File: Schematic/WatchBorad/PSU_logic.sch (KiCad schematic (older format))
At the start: 37 parts, among them J3 TYPE-C-31-M-17, SW1 SW_Push, SW2 SW_Push, U10 M41T62Q6F, U5 BQ21040DBVT, U6 MAX17048G+T10, U7 max16054azt+t, U8 TPS2113APWR, Y1 Crystal_Small

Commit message: Added missed resistors to the lcsc [SCHEMATIC][BOM]
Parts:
- R1, R15, R16, R17, R18, R2, R20, R21, R23, R24: lcsc (none) -> https://www.lcsc.com/product-detail/Chip-Resistor-Surface-M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
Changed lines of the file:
@@
 F 2 "Resistor_SMD:R_0603_1608Metric" V 4430 1350 50  0001 C CNN
 F 3 "~" H 4500 1350 50  0001 C CNN
+F 4 "https://www.lcsc.com/product-detail/Chip-Resistor-Surface-Mount_YAGEO-RC0603FR-0710KL_C98220.html" H 4500 1350 50  0001 C CNN "lcsc"
 	1    4500 1350
 	0    1    1    0
@@
 F 2 "Resistor_SMD:R_0603_1608Metric" V 2380 2650 50  0001 C CNN
 F 3 "~" H 2450 2650 50  0001 C CNN
+F 4 "https://www.lcsc.com/product-detail/Chip-Resistor-Surface-Mount_YAGEO-RC0603FR-0710KL_C98220.html" H 2450 2650 50  0001 C CNN "lcsc"
 	1    2450 2650
 	-1   0    0    1
@@
 F 2 "Resistor_SMD:R_0603_1608Metric" V 2555 1975 50  0001 C CNN
 F 3 "~" H 2625 1975 50  0001 C CNN
+F 4 "https://www.lcsc.com/product-detail/Chip-Resistor-Surface-Mount_YAGEO-RC0603FR-0710KL_C98220.html" H 2625 1975 50  0001 C CNN "lcsc"
 	1    2625 1975
 	-1   0    0    1
@@
 F 2 "Resistor_SMD:R_0603_1608Metric" V 7955 6075 50  0001 C CNN
 F 3 "https://lcsc.com/product-detail/Others_Viking-Tech-ARG03FTC3300_C217969.html" H 8025 6075 50  0001 C CNN
+F 4 "https://www.lcsc.com/product-detail/Chip-Resistor-Surface-Mount_Walsin-Tech-Corp-WR06X331JTL_C384242.html" H 8025 6075 50  0001 C CNN "lcsc"
 	1    8025 6075
 	0    1    1    0
@@
 F 2 "Resistor_SMD:R_0603_1608Metric" V 2680 4850 50  0001 C CNN
 F 3 "~" H 2750 4850 50  0001 C CNN
+F 4 "https://www.lcsc.com/product-detail/Chip-Resistor-Surface-Mount_YAGEO-RC0603FR-0710KL_C98220.html" H 2750 4850 50  0001 C CNN "lcsc"
 	1    2750 4850
 	0    1    -1   0
@@
 F 2 "Resistor_SMD:R_0603_1608Metric" V 4955 4800 50  0001 C CNN
 F 3 "~" H 5025 4800 50  0001 C CNN
+F 4 "https://www.lcsc.com/product-detail/Chip-Resistor-Surface-Mount_YAGEO-RC0603FR-0710KL_C98220.html" H 5025 4800 50  0001 C CNN "lcsc"
 	1    5025 4800
 	1    0    0    1
@@
 F 2 "Resistor_SMD:R_0603_1608Metric" V 1405 1725 50  0001 C CNN
 F 3 "https://lcsc.com/product-detail/Others_Viking-Tech-ARG03FTC3300_C217969.html" H 1475 1725 50  0001 C CNN
+F 4 "https://www.lcsc.com/product-detail/Chip-Resistor-Surface-Mount_Walsin-Tech-Corp-WR06X331JTL_C384242.html" H 1475 1725 50  0001 C CNN "lcsc"
 	1    1475 1725
 	0    1    1    0
@@
 F 2 "Resistor_SMD:R_0603_1608Metric" V 1405 2350 50  0001 C CNN
 F 3 "https://lcsc.com/product-detail/Others_Viking-Tech-ARG03FTC3300_C217969.html" H 1475 2350 50  0001 C CNN
+F 4 "https://www.lcsc.com/product-detail/Chip-Resistor-Surface-Mount_Walsin-Tech-Corp-WR06X331JTL_C384242.html" H 1475 2350 50  0001 C CNN "lcsc"
 	1    1475 2350
 	0    1    1    0
@@
 F 2 "Resistor_SMD:R_0603_1608Metric" V 10305 2400 50  0001 C CNN
 F 3 "~" H 10375 2400 50  0001 C CNN
+F 4 "https://www.lcsc.com/product-detail/Chip-Resistor-Surface-Mount_YAGEO-RC0603FR-0710KL_C98220.html" H 10375 2400 50  0001 C CNN "lcsc"
 	1    10375 2400
 	1    0    0    -1
@@
 F 2 "Resistor_SMD:R_0603_1608Metric" V 8255 2300 50  0001 C CNN
 F 3 "~" H 8325 2300 50  0001 C CNN
+F 4 "https://www.lcsc.com/product-detail/Chip-Resistor-Surface-Mount_YAGEO-RC0603FR-0710KL_C98220.html" H 8325 2300 50  0001 C CNN "lcsc"
 	1    8325 2300
 	1    0    0    -1

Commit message: Added D-trigger instead of the MAX switching chip
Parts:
- removed U7: max16054azt+t, TO_SOT_Packages_SMD:SOT-23-6_Handsoldering, symbol OnOffControllers:max16054azt+t
- added C8: 100 nF, Capacitor_SMD:C_0603_1608Metric, symbol Device:C
- added U7: SN74LVC2G74-EP_DCU_8, SN74LVC2G74:SN74LVC2G74, symbol SN74LVC2G74:SN74LVC2G74-EP_DCU_8
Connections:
- wire segments 147 -> 158
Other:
- note removed: "Int 63KOhm PU\n"
- moved on the sheet: C29, R21, TP11, TP20

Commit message: Removed redundant symbols descriptions from schematic [SCHEMATIC]
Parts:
- U10: MPN M41T62Q6F -> (none); OC_FARNELL 1224441 -> (none); OC_NEWARK 56P9316 -> (none); PACKAGE QFN-16 -> (none); SUPPLIER STMICROELECTRONICS -> (none)
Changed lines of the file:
@@
 F 2 "QFN50P300X300X100-17N" H 9475 3050 50  0001 L BNN
 F 3 "https://datasheet.lcsc.com/lcsc/1806121917_STMicroelectronics-M41T62Q6F_C113207.pdf" H 9475 3050 50  0001 L BNN
-F 4 "M41T62Q6F" H 9475 3050 50  0001 L BNN "MPN"
-F 5 "1224441" H 9475 3050 50  0001 L BNN "OC_FARNELL"
-F 6 "56P9316" H 9475 3050 50  0001 L BNN "OC_NEWARK"
-F 7 "QFN-16" H 9475 3050 50  0001 L BNN "PACKAGE"
-F 8 "STMICROELECTRONICS" H 9475 3050 50  0001 L BNN "SUPPLIER"
-F 9 "https://lcsc.com/product-detail/Real-time-Clocks-span-style-background-color-ff0-RTC-span_STMicroelectronics-M41T62Q6F_C113207.html" H 9475 3050 50  0001 C CNN "lcsc"
+F 4 "https://lcsc.com/product-detail/Real-time-Clocks-span-style-background-color-ff0-RTC-span_STMicroelectronics-M41T62Q6F_C113207.html" H 9475 3050 50  0001 C CNN "lcsc"
 	1    9475 3050
 	1    0    0    -1

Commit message: Fixed D-trigger routing around the switching circuit [PCB]
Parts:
- added R22, R25: 10k, Resistor_SMD:R_0603_1608Metric, symbol Device:R
- C8: value 100 nF -> 10 uF
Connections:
- wire segments 158 -> 164
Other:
- moved on the sheet: C29, C8, R21
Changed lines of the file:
@@
 L Device:C C?
 U 1 1 5F943E27
-P 7110 1300
+P 7630 1300
 AR Path="/5EA4867C/5F943E27" Ref="C?"  Part="1"
 AR Path="/5E9C1C3A/5F943E27" Ref="C?"  Part="1"
 AR Path="/5ED3F98E/5F943E27" Ref="C?"  Part="1"
 AR Path="/5F913559/5F943E27" Ref="C29"  Part="1"
-F 0 "C29" H 7135 1375 50  0000 L CNN
-F 1 "100 nF" V 6960 1175 50  0000 L CNN
-F 2 "Capacitor_SMD:C_0603_1608Metric" H 7148 1150 50  0001 C CNN
-F 3 "~" H 7110 1300 50  0001 C CNN
-F 4 "https://lcsc.com/product-detail/Multilayer-Ceramic-Capacitors-MLCC-SMD-SMT_YAGEO-CC0603KRX7R9BB104_C14663.html" H 7110 1300 50  0001 C CNN "lcsc"
-	1    7110 1300
+F 0 "C29" H 7655 1375 50  0000 L CNN
+F 1 "100 nF" V 7480 1175 50  0000 L CNN
+F 2 "Capacitor_SMD:C_0603_1608Metric" H 7668 1150 50  0001 C CNN
+F 3 "~" H 7630 1300 50  0001 C CNN
+F 4 "https://lcsc.com/product-detail/Multilayer-Ceramic-Capacitors-MLCC-SMD-SMT_YAGEO-CC0603KRX7R9BB104_C14663.html" H 7630 1300 50  0001 C CNN "lcsc"
+	1    7630 1300
 	0    -1   -1   0
 $EndComp
-Text Label 6420 1300 0    50   ~ 0
+Text Label 6940 1300 0    50   ~ 0
 V_Battery_P
 Wire Notes Line
@@
 L power:GND #PWR?
 U 1 1 5F943EB2
-P 7000 2600
+P 6800 2740
 AR Path="/5F943EB2" Ref="#PWR?"  Part="1"
 AR Path="/5E9B1DCE/5F943EB2" Ref="#PWR?"  Part="1"
 AR Path="/5ED3F98E/5F943EB2" Ref="#PWR?"  Part="1"
 AR Path="/5F913559/5F943EB2" Ref="#PWR035"  Part="1"
-F 0 "#PWR035" H 7000 2350 50  0001 C CNN
-F 1 "GND" H 7000 2450 50  0000 C CNN
-F 2 "" H 7000 2600 50  0001 C CNN
-F 3 "" H 7000 2600 50  0001 C CNN
-	1    7000 2600
+F 0 "#PWR035" H 6800 2490 50  0001 C CNN
+F 1 "GND" H 6800 2590 50  0000 C CNN
+F 2 "" H 6800 2740 50  0001 C CNN
+F 3 "" H 6800 2740 50  0001 C CNN
+	1    6800 2740
 	1    0    0    -1
 $EndComp
@@
 L power:+BATT #PWR?
 U 1 1 5F9B18FF
-P 6900 1140
+P 7420 1140
 AR Path="/5E9C1C3A/5F9B18FF" Ref="#PWR?"  Part="1"
 AR Path="/5F7F86D0/5F9B18FF" Ref="#PWR?"  Part="1"
 AR Path="/5ED3F98E/5F9B18FF" Ref="#PWR?"  Part="1"
 AR Path="/5F913559/5F9B18FF" Ref="#PWR036"  Part="1"
-F 0 "#PWR036" H 6900 990 50  0001 C CNN
-F 1 "+BATT" H 6915 1313 50  0000 C CNN
-F 2 "" H 6900 1140 50  0001 C CNN
-F 3 "" H 6900 1140 50  0001 C CNN
-	1    6900 1140
+F 0 "#PWR036" H 7420 990 50  0001 C CNN
+F 1 "+BATT" H 7435 1313 50  0000 C CNN
+F 2 "" H 7420 1140 50  0001 C CNN
+F 3 "" H 7420 1140 50  0001 C CNN
+	1    7420 1140
 	-1   0    0    -1
 $EndComp
@@
 	6840 3340 6840 3520
 Wire Wire Line
-	3150 1300 4170 1300
-Wire Wire Line
 	3150 1300 3150 1525
 $Comp
 L power:GND #PWR0102
 U 1 1 6187DAB4
-P 7360 1300
-F 0 "#PWR0102" H 7360 1050 50  0001 C CNN
-F 1 "GND" H 7365 1127 50  0000 C CNN
-F 2 "" H 7360 1300 50  0001 C CNN
-F 3 "" H 7360 1300 50  0001 C CNN
-	1    7360 1300
+P 7880 1300
+F 0 "#PWR0102" H 7880 1050 50  0001 C CNN
+F 1 "GND" H 7885 1127 50  0000 C CNN
+F 2 "" H 7880 1300 50  0001 C CNN
+F 3 "" H 7880 1300 50  0001 C CNN
+	1    7880 1300
 	0    -1   -1   0
 $EndComp
@@
 	4100 1400 4170 1400
 Wire Wire Line
-	6370 1300 6900 1300
-Wire Wire Line
-	6900 1140 6900 1300
-Connection ~ 6900 1300
-Wire Wire Line
-	6900 1300 6960 1300
-Wire Wire Line
-	7260 1300 7360 1300
+	7420 1140 7420 1300
+Connection ~ 7420 1300
+Wire Wire Line
+	7420 1300 7480 1300
+Wire Wire Line
+	7780 1300 7880 1300
 $Comp
 L Connector:TestPoint TP?
@@
 L Device:C C8
 U 1 1 6189A4CE
-P 7000 2350
-F 0 "C8" H 7115 2396 50  0000 L CNN
-F 1 "100 nF" H 7115 2305 50  0000 L CNN
-F 2 "Capacitor_SMD:C_0603_1608Metric" H 7038 2200 50  0001 C CNN
-F 3 "~" H 7000 2350 50  0001 C CNN
-F 4 "https://lcsc.com/product-detail/Multilayer-Ceramic-Capacitors-MLCC-SMD-SMT_YAGEO-CC0603KRX7R9BB104_C14663.html" H 7000 2350 50  0001 C CNN "lcsc"
-	1    7000 2350
+P 6800 2490
+F 0 "C8" H 6915 2536 50  0000 L CNN
+F 1 "10 uF" H 6915 2445 50  0000 L CNN
+F 2 "Capacitor_SMD:C_0603_1608Metric" H 6838 2340 50  0001 C CNN
+F 3 "~" H 6800 2490 50  0001 C CNN
+F 4 "https://lcsc.com/product-detail/Multilayer-Ceramic-Capacitors-MLCC-SMD-SMT_YAGEO-CC0603KRX7R9BB104_C14663.html" H 6800 2490 50  0001 C CNN "lcsc"
+	1    6800 2490
 	1    0    0    -1
 $EndComp
@@
 L Device:R R?
 U 1 1 5F943E4B
-P 6660 2110
+P 6800 2100
 AR Path="/5EA4867C/5F943E4B" Ref="R?"  Part="1"
 AR Path="/5ED3F98E/5F943E4B" Ref="R?"  Part="1"
 AR Path="/5F913559/5F943E4B" Ref="R21"  Part="1"
-F 0 "R21" V 6560 1910 50  0000 L CNN
-F 1 "10k" V 6560 2210 50  0000 L CNN
-F 2 "Resistor_SMD:R_0603_1608Metric" V 6590 2110 50  0001 C CNN
-F 3 "~" H 6660 2110 50  0001 C CNN
-F 4 "https://www.lcsc.com/product-detail/Chip-Resistor-Surface-Mount_YAGEO-RC0603FR-0710KL_C98220.html" H 6660 2110 50  0001 C CNN "lcsc"
-	1    6660 2110
-	0    1    1    0
+F 0 "R21" V 6700 1900 50  0000 L CNN
+F 1 "10k" V 6700 2200 50  0000 L CNN
+F 2 "Resistor_SMD:R_0603_1608Metric" V 6730 2100 50  0001 C CNN
+F 3 "~" H 6800 2100 50  0001 C CNN
+F 4 "https://www.lcsc.com/product-detail/Chip-Resistor-Surface-Mount_YAGEO-RC0603FR-0710KL_C98220.html" H 6800 2100 50  0001 C CNN "lcsc"
+	1    6800 2100
+	-1   0    0    1
 $EndComp
 $Comp
 L power:+BATT #PWR0106
 U 1 1 61996A40
-P 7000 2050
-F 0 "#PWR0106" H 7000 1900 50  0001 C CNN
-F 1 "+BATT" H 7015 2223 50  0000 C CNN
-F 2 "" H 7000 2050 50  0001 C CNN
-F 3 "" H 7000 2050 50  0001 C CNN
-	1    7000 2050
-	1    0    0    -1
-$EndComp
-Wire Wire Line
-	6450 1500 6450 2110
-Wire Wire Line
-	6450 2110 6510 2110
+P 6800 1910
+F 0 "#PWR0106" H 6800 1760 50  0001 C CNN
+F 1 "+BATT" H 6815 2083 50  0000 C CNN
+F 2 "" H 6800 1910 50  0001 C CNN
+F 3 "" H 6800 1910 50  0001 C CNN
+	1    6800 1910
+	1    0    0    -1
+$EndComp
 Wire Wire Line
 	6370 1500 6450 1500
 Wire Wire Line
-	7000 2110 7000 2200
-Wire Wire Line
-	6810 2110 7000 2110
-Wire Wire Line
-	7000 2110 7000 2050
-Connection ~ 7000 2110
-Wire Wire Line
-	7000 2500 7000 2600
+	6800 2640 6800 2740
 $Comp
 L SN74LVC2G74:SN74LVC2G74-EP_DCU_8 U7
@@
 	1    0    0    -1
 $EndComp
+$Comp
+L Device:R R22
+U 1 1 617EFB8E
+P 3690 1110
+F 0 "R22" H 3760 1156 50  0000 L CNN
+F 1 "10k" H 3760 1065 50  0000 L CNN
+F 2 "Resistor_SMD:R_0603_1608Metric" V 3620 1110 50  0001 C CNN
+F 3 "~" H 3690 1110 50  0001 C CNN
+F 4 "https://www.lcsc.com/product-detail/Chip-Resistor-Surface-Mount_YAGEO-RC0603FR-0710KL_C98220.html" H 3690 1110 50  0001 C CNN "lcsc"
+	1    3690 1110
+	1    0    0    -1
+$EndComp
+$Comp
+L power:+BATT #PWR043
+U 1 1 617FFD22
+P 3690 910
+F 0 "#PWR043" H 3690 760 50  0001 C CNN
+F 1 "+BATT" H 3705 1083 50  0000 C CNN
+F 2 "" H 3690 910 50  0001 C CNN
+F 3 "" H 3690 910 50  0001 C CNN
+	1    3690 910
+	1    0    0    -1
+$EndComp
+Wire Wire Line
+	3150 1300 3690 1300
+Wire Wire Line
+	3690 1260 3690 1300
+Connection ~ 3690 1300
+Wire Wire Line
+	3690 1300 4170 1300
+Wire Wire Line
+	3690 910  3690 960
+Wire Wire Line
+	6800 1910 6800 1950
+Wire Wire Line
+	6450 2290 6800 2290
+Wire Wire Line
+	6800 2290 6800 2250
+Wire Wire Line
+	6450 1500 6450 2290
+Wire Wire Line
+	6800 2290 6800 2340
+Connection ~ 6800 2290
+$Comp
+L Device:R R25
+U 1 1 61851142
+P 6480 1090
+F 0 "R25" H 6550 1136 50  0000 L CNN
+F 1 "10k" H 6550 1045 50  0000 L CNN
+F 2 "Resistor_SMD:R_0603_1608Metric" V 6410 1090 50  0001 C CNN
+F 3 "~" H 6480 1090 50  0001 C CNN
+F 4 "https://www.lcsc.com/product-detail/Chip-Resistor-Surface-Mount_YAGEO-RC0603FR-0710KL_C98220.html" H 6480 1090 50  0001 C CNN "lcsc"
+	1    6480 1090
+	1    0    0    -1
+$EndComp
+Wire Wire Line
+	6370 1300 7420 1300
+Wire Wire Line
+	6370 1400 6480 1400
+$Comp
+L power:+BATT #PWR059
+U 1 1 61870E94
+P 6480 890
+F 0 "#PWR059" H 6480 740 50  0001 C CNN
+F 1 "+BATT" H 6495 1063 50  0000 C CNN
+F 2 "" H 6480 890 50  0001 C CNN
+F 3 "" H 6480 890 50  0001 C CNN
+	1    6480 890
+	1    0    0    -1
+$EndComp
+Wire Wire Line
+	6480 940  6480 890
+Wire Wire Line
+	6480 1400 6480 1240
 $EndSCHEMATC

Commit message: Changed Power MUX circuit to the transistors
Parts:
- removed C30, C31: 100 nF, Capacitor_SMD:C_0603_1608Metric, symbol Device:C
- removed U8: TPS2113APWR, LocalFootprints:TPS2115APWR, symbol WatchBorad-rescue:TPS2113APWR-PowerMuxes-WatchBorad-rescue-WatchBorad-rescue
- added D3: D, Diode_SMD:D_0603_1608Metric_Pad1.05x0.95mm_HandSolder, symbol Device:D
- added R34: 10K, Resistor_SMD:R_0603_1608Metric, symbol Device:R
- added VT3, VT5: HX2301A, Package_TO_SOT_SMD:SOT-23, symbol MosfetLocal:HX2301A
- R24: value 330 -> 1K; lcsc https://www.lcsc.com/product-detail/Chip-Resistor-Surface-Mount_Walsin-Tech-Corp-WR06X331JTL_C384242.html -> https://www.lcsc.com/product-detail/Chip-Resistor-Surface-Mount_YAGEO-RC0603FR-0710KL_C98220.html
- VT1, VT2: footprint TO_SOT_Packages_SMD:SOT-23 -> Package_TO_SOT_SMD:SOT-23
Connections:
- net labels removed: Rlim
- wire segments 164 -> 163
- no-connect marks 6 -> 5
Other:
- note removed: "1.5A\n"
- note removed: "EN| VSNS | VI(IN2) > VI(IN1) | OUT\n0 |<0.8V |No |IN1\n0 |<0.8V |Yes |IN2"
- moved on the sheet: TP12

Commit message: Added ME4055A charger instead of BQ21040DBVR
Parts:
- removed R23: 10k, Resistor_SMD:R_0603_1608Metric, symbol Device:R
- removed U5: BQ21040DBVT, TO_SOT_Packages_SMD:SOT-23-6, symbol BatteryManagmentLocal:BQ21040DBVT
- added U5: ME4055A, Package_TO_SOT_SMD:SOT-23-6, symbol BatteryManagmentLocal:ME4055A
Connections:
- wire segments 163 -> 160
- no-connect marks 5 -> 6
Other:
- note added: "Set fast charge\ncurrent to +-120 mA"
- note removed: "Set fast charge\ncurrent to 54 mA"
- moved on the sheet: C28, R20

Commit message: Fixed D3 footpint [SCHEMATIC][PCB]
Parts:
- D3: footprint Diode_SMD:D_0603_1608Metric_Pad1.05x0.95mm_HandSolder -> Diode_SMD:D_SOD-323
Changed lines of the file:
@@
 F 0 "D3" H 8270 4813 50  0000 C CNN
 F 1 "D" H 8270 4904 50  0000 C CNN
-F 2 "Diode_SMD:D_0603_1608Metric_Pad1.05x0.95mm_HandSolder" H 8270 5030 50  0001 C CNN
+F 2 "Diode_SMD:D_SOD-323" H 8270 5030 50  0001 C CNN
 F 3 "https://datasheet.lcsc.com/lcsc/1810202112_Guangdong-Hottech-1N5819WS_C191023.pdf" H 8270 5030 50  0001 C CNN
 F 4 "https://lcsc.com/product-detail/Schottky-Barrier-Diodes-SBD_Guangdong-Hottech-1N5819WS_C191023.html" H 8270 5030 50  0001 C CNN "lcsc"

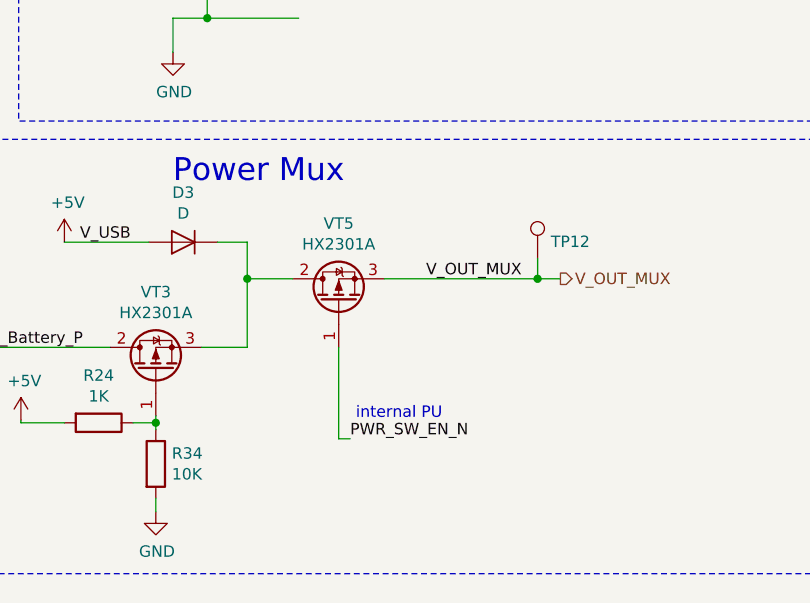
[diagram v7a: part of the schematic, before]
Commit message: Fixed Transistor position in PSU_Logic POwer MUX [PCB] [SCHEMATIC]
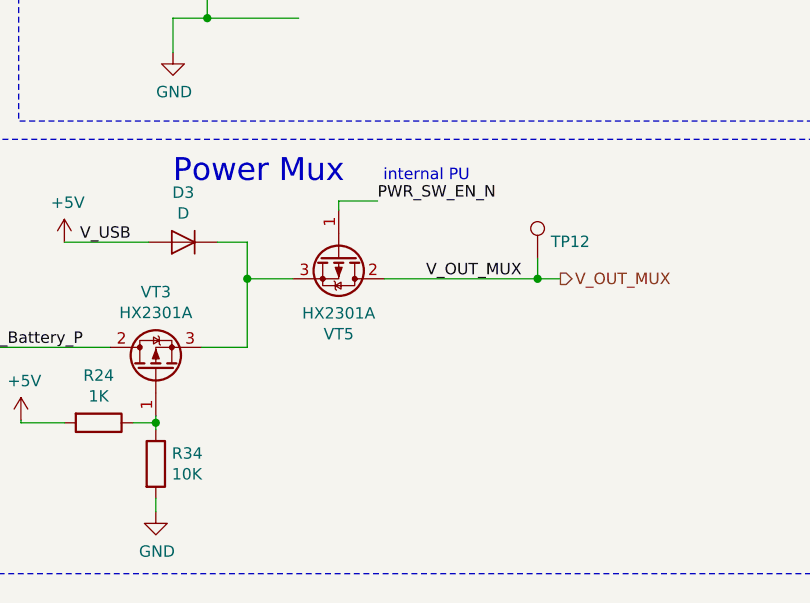
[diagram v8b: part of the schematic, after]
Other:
- moved on the sheet: VT5
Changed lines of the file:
@@
 Wire Wire Line
 	1550 4250 1775 4250
-Text Notes 9025 5810 0    50   ~ 0
+Text Notes 9145 4770 0    50   ~ 0
 internal PU\n
 Wire Notes Line
@@
 L MosfetLocal:HX2301A VT5
 U 1 1 618EF835
-P 8950 5290
-F 0 "VT5" V 9292 5290 50  0000 C CNN
-F 1 "HX2301A" V 9201 5290 50  0000 C CNN
-F 2 "Package_TO_SOT_SMD:SOT-23" H 9150 5390 50  0001 C CNN
-F 3 "https://lcsc.com/product-detail/MOSFETs_HX-hengjiaxing-HX2301A_C296298.html" H 8950 5290 50  0001 C CNN
-F 4 "https://lcsc.com/product-detail/MOSFETs_HX-hengjiaxing-HX2301A_C296298.html" V 8950 5290 50  0001 C CNN "lcsc"
-	1    8950 5290
-	0    -1   -1   0
-$EndComp
-Text Label 9000 5890 0    50   ~ 0
+P 8950 5090
+F 0 "VT5" V 9292 5090 50  0000 C CNN
+F 1 "HX2301A" V 9201 5090 50  0000 C CNN
+F 2 "Package_TO_SOT_SMD:SOT-23" H 9150 5190 50  0001 C CNN
+F 3 "https://lcsc.com/product-detail/MOSFETs_HX-hengjiaxing-HX2301A_C296298.html" H 8950 5090 50  0001 C CNN
+F 4 "https://lcsc.com/product-detail/MOSFETs_HX-hengjiaxing-HX2301A_C296298.html" V 8950 5090 50  0001 C CNN "lcsc"
+	1    8950 5090
+	0    1    1    0
+$EndComp
+Text Label 9120 4850 0    50   ~ 0
 PWR_SW_EN_N
-Wire Wire Line
-	8950 5490 8950 5890
-Wire Wire Line
-	8950 5890 9000 5890
 Wire Wire Line
 	8350 5490 8550 5490
@@
 Wire Wire Line
 	4830 4340 4650 4340
+Wire Wire Line
+	9120 4850 8950 4850
+Wire Wire Line
+	8950 4850 8950 4890
 $EndSCHEMATC
